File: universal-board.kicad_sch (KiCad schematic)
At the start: 38 parts, among them J1 USB_C_Receptacle, J2 Conn_02x04_Odd_Even, J3 Conn_01x08, J4 CONN_WS2812, J5 CONN_I2C_GROVE, Q1 BSS138, SW1 SW_RESET, SW2 SW_ACK, U1 USBLC6-2SC6, U2 AMS1117-3.3, U3 CH224K, U4 USBLC6-2SC6, U5 74AHCT1G125, U6 TSOP384xx, U7 ESP32-S3-WROOM-1

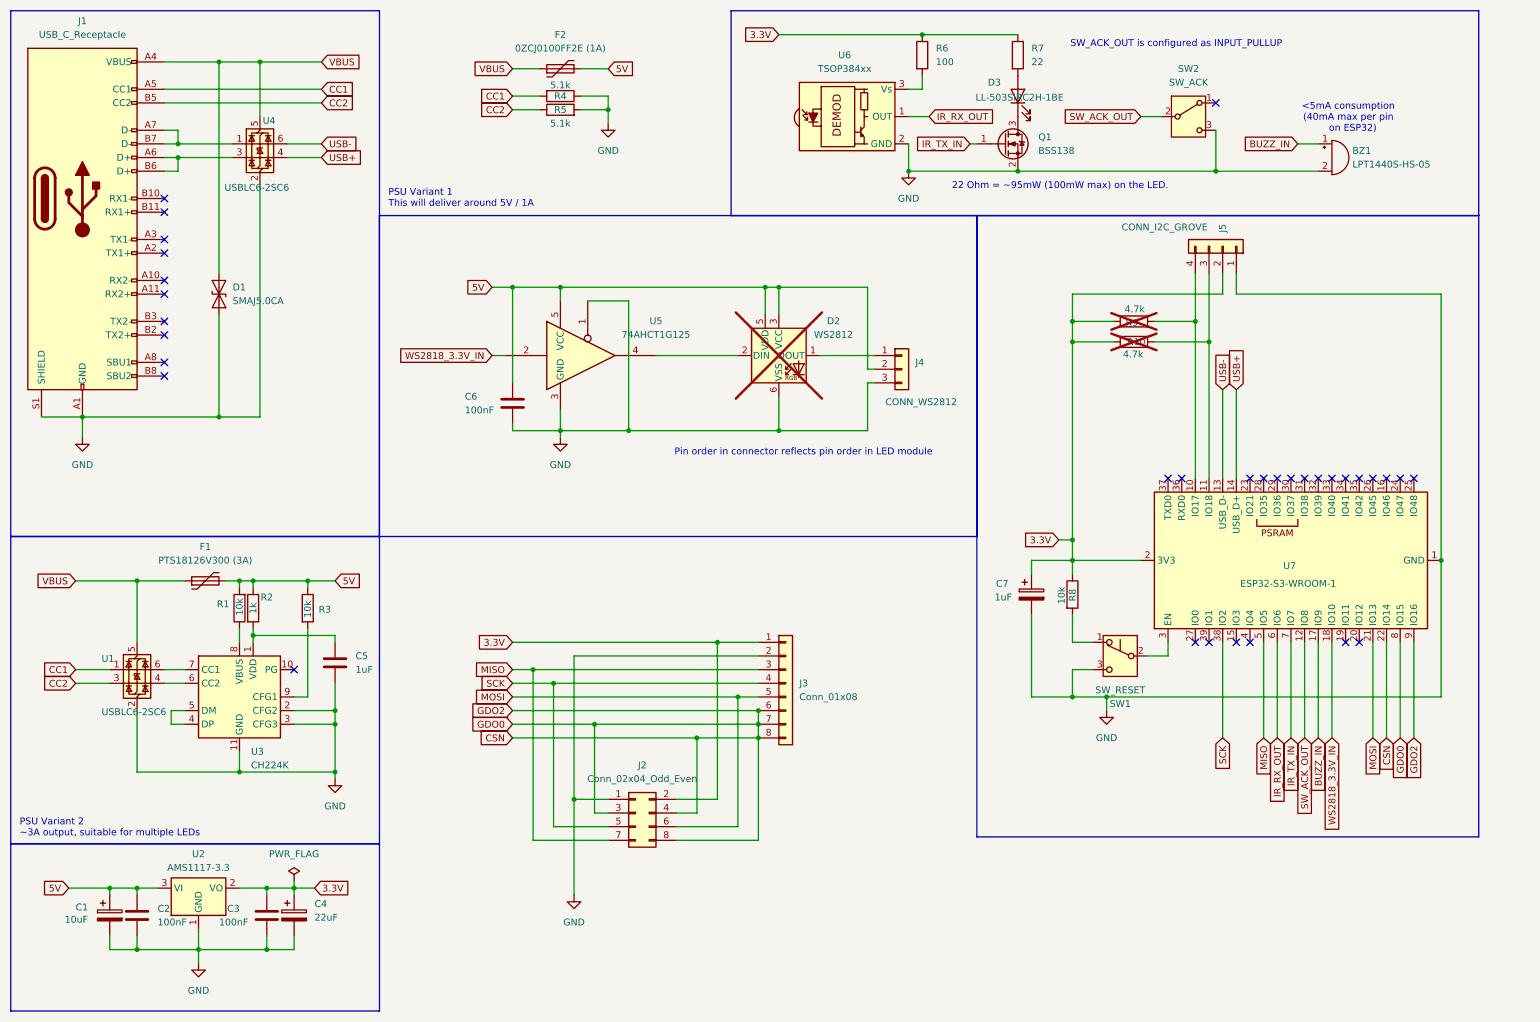
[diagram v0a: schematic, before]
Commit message: ERC checks clean.
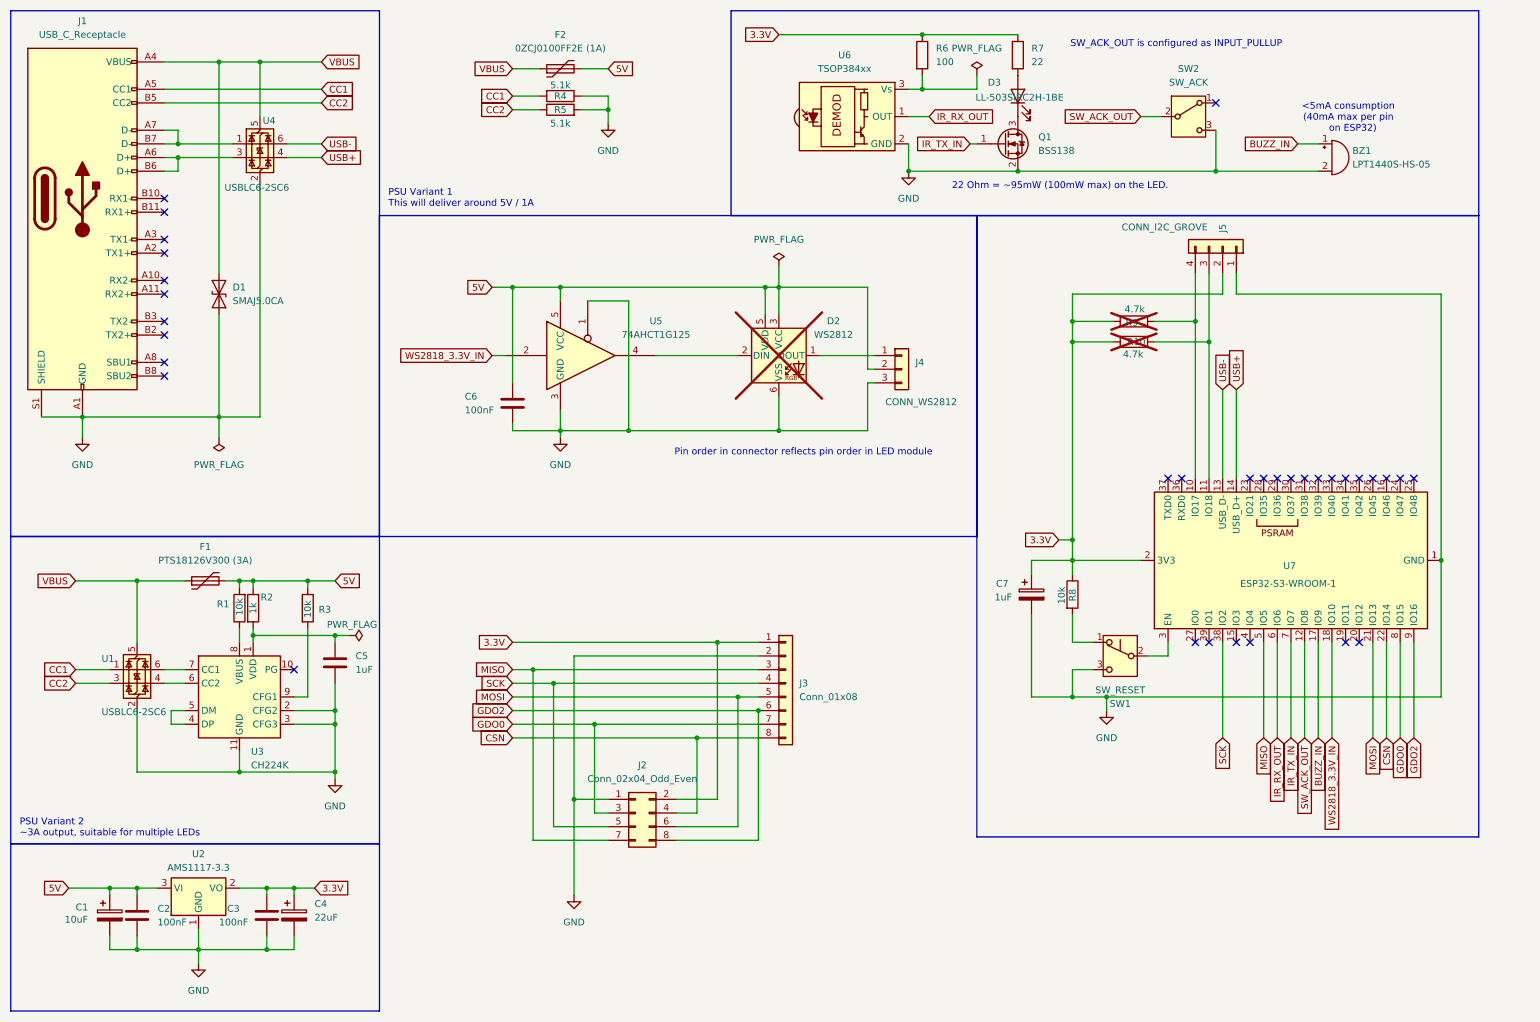
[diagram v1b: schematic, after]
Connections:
- net CSN: no longer J2.3 (Pin_3), J2.8 (Pin_8), J3.6 (Pin_6), J3.7 (Pin_7), U7.8 (IO15), U7.9 (IO16)
- new net GDO0: J2.3 (Pin_3), J3.7 (Pin_7), U7.8 (IO15)
- new net GDO2: J2.8 (Pin_8), J3.6 (Pin_6), U7.9 (IO16)

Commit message: Rev 1, added test points
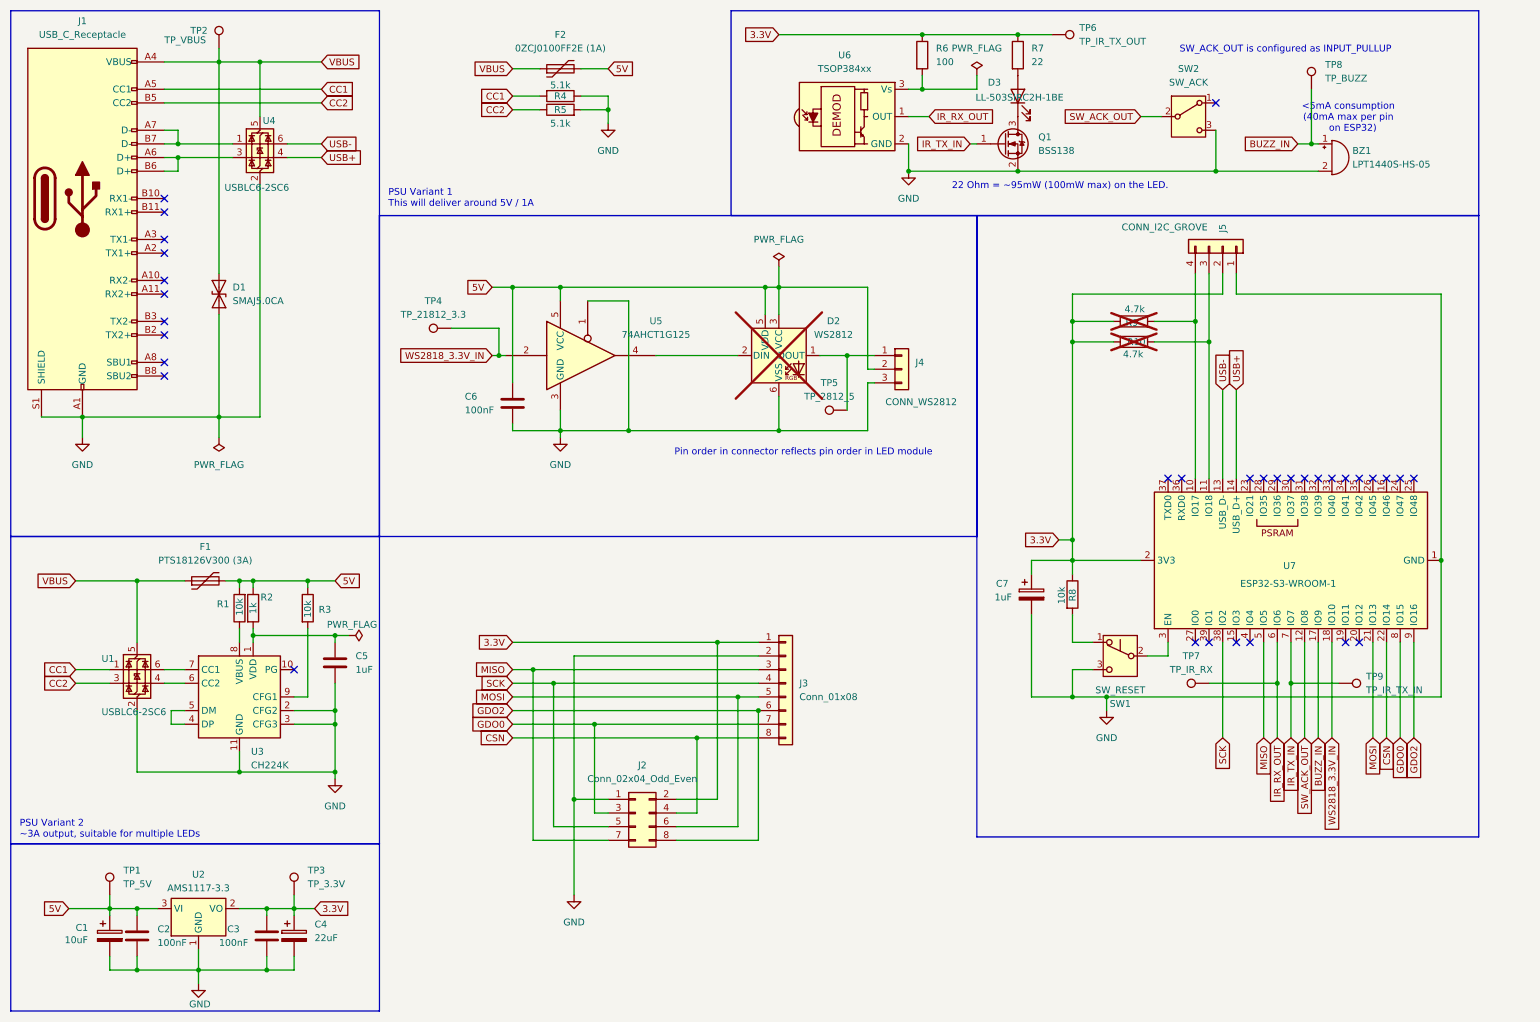
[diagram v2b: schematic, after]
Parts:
- added TP1: TP_5V, symbol Connector:TestPoint
- added TP2: TP_VBUS, symbol Connector:TestPoint
- added TP3: TP_3.3V, symbol Connector:TestPoint
- added TP4: TP_21812_3.3, symbol Connector:TestPoint
- added TP5: TP_2812_5, symbol Connector:TestPoint
- added TP6: TP_IR_TX_OUT, symbol Connector:TestPoint
- added TP7: TP_IR_RX, symbol Connector:TestPoint
- added TP8: TP_BUZZ, symbol Connector:TestPoint
- added TP9: TP_IR_TX_IN, symbol Connector:TestPoint
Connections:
- net 3.3V: now also TP3.1, TP6.1
- net 5V: now also TP1.1
- net BUZZ_IN: now also TP8.1
- net IR_RX_OUT: now also TP7.1
- net IR_TX_IN: now also TP9.1
- net VBUS: now also TP2.1
- net WS2818_3.3V_IN: now also TP4.1
- net at D2.1 (DOUT), J4.1 (Pin_1): now also TP5.1
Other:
- title: (none) -> esphome universal board
- moved on the sheet: C1, C2, C3, C4, U2

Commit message: Partial footprint assignment.
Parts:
- BZ1: footprint (none) -> Buzzer_Beeper:MagneticBuzzer_CUI_CST-931RP-A
- C1: footprint (none) -> Capacitor_THT:CP_Radial_D6.3mm_P2.50mm
- C2, C3, C5, C6, R1, R10, R2, R3, R4, R5, R6, R7, R8, R9: footprint (none) -> Capacitor_SMD:C_1206_3216Metric_Pad1.33x1.80mm_HandSolder
- C4: footprint (none) -> Capacitor_THT:CP_Radial_D5.0mm_P2.00mm
- C7: footprint (none) -> Capacitor_THT:CP_Radial_D5.0mm_P2.50mm
- D3: footprint (none) -> LED_THT:LED_D5.0mm_Clear
- F1: footprint (none) -> Fuse:Fuse_1812_4532Metric_Pad1.30x3.40mm_HandSolder
- F2: footprint (none) -> Fuse:Fuse_1206_3216Metric_Pad1.42x1.75mm_HandSolder
- SW1, SW2: footprint (none) -> Button_Switch_THT:SW_PUSH_6mm
- TP1, TP2, TP3, TP4, TP5, TP6, TP7, TP8, TP9: footprint (none) -> TestPoint:TestPoint_Pad_D2.0mm
- U5: footprint (none) -> Package_TO_SOT_SMD:SOT-353_SC-70-5_Handsoldering
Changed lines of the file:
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@@
 			)
 		)
-		(property "Footprint" ""
+		(property "Footprint" "Capacitor_SMD:C_1206_3216Metric_Pad1.33x1.80mm_HandSolder"
 			(at 207.772 120.65 90)
 			(effects
@@
 			)
 		)
-		(property "Footprint" ""
+		(property "Footprint" "Fuse:Fuse_1206_3216Metric_Pad1.42x1.75mm_HandSolder"
 			(at 119.38 21.59 0)
 			(effects
@@
 			)
 		)
-		(property "Footprint" ""
+		(property "Footprint" "LED_THT:LED_D5.0mm_Clear"
 			(at 199.39 27.94 0)
 			(effects
@@
 			)
 		)
-		(property "Footprint" ""
+		(property "Footprint" "Button_Switch_THT:SW_PUSH_6mm"
 			(at 231.14 31.75 0)
 			(effects
@@
 			)
 		)
-		(property "Footprint" ""
+		(property "Footprint" "Capacitor_THT:CP_Radial_D6.3mm_P2.50mm"
 			(at 31.4452 187.96 0)
 			(effects
@@
 			)
 		)
-		(property "Footprint" ""
+		(property "Footprint" "Fuse:Fuse_1812_4532Metric_Pad1.30x3.40mm_HandSolder"
 			(at 53.34 116.84 0)
 			(effects
@@
 			)
 		)
-		(property "Footprint" ""
+		(property "Footprint" "Button_Switch_THT:SW_PUSH_6mm"
 			(at 218.44 132.08 0)
 			(effects
@@
 			)
 		)
-		(property "Footprint" ""
+		(property "Footprint" "TestPoint:TestPoint_Pad_D2.0mm"
 			(at 55.88 19.05 0)
 			(effects
@@
 			)
 		)
-		(property "Footprint" ""
+		(property "Footprint" "TestPoint:TestPoint_Pad_D2.0mm"
 			(at 205.74 21.59 0)
 			(effects
@@
 			)
 		)
-		(property "Footprint" ""
+		(property "Footprint" "Capacitor_SMD:C_1206_3216Metric_Pad1.33x1.80mm_HandSolder"
 			(at 106.3752 88.9 0)
 			(effects
@@
 			)
 		)
-		(property "Footprint" ""
+		(property "Footprint" "Capacitor_SMD:C_1206_3216Metric_Pad1.33x1.80mm_HandSolder"
 			(at 197.612 20.32 90)
 			(effects
@@
 			)
 		)
-		(property "Footprint" ""
+		(property "Footprint" "TestPoint:TestPoint_Pad_D2.0mm"
 			(at 69.85 176.53 0)
 			(effects
@@
 			)
 		)
-		(property "Footprint" ""
+		(property "Footprint" "Capacitor_SMD:C_1206_3216Metric_Pad1.33x1.80mm_HandSolder"
 			(at 55.372 123.19 90)
 			(effects
@@
 			)
 		)
-		(property "Footprint" ""
+		(property "Footprint" "Capacitor_SMD:C_1206_3216Metric_Pad1.33x1.80mm_HandSolder"
 			(at 220.98 71.628 90)
 			(effects
@@
 			)
 		)
-		(property "Footprint" ""
+		(property "Footprint" "Capacitor_SMD:C_1206_3216Metric_Pad1.33x1.80mm_HandSolder"
 			(at 60.6552 187.96 0)
 			(effects
@@
 			)
 		)
-		(property "Footprint" ""
+		(property "Footprint" "Capacitor_SMD:C_1206_3216Metric_Pad1.33x1.80mm_HandSolder"
 			(at 220.98 71.882 90)
 			(effects
@@
 			)
 		)
-		(property "Footprint" ""
+		(property "Footprint" "TestPoint:TestPoint_Pad_D2.0mm"
 			(at 259.08 26.67 0)
 			(effects
@@
 			)
 		)
-		(property "Footprint" ""
+		(property "Footprint" "Capacitor_SMD:C_1206_3216Metric_Pad1.33x1.80mm_HandSolder"
 			(at 56.388 123.19 90)
 			(effects
@@
 			)
 		)
-		(property "Footprint" ""
+		(property "Footprint" "Capacitor_SMD:C_1206_3216Metric_Pad1.33x1.80mm_HandSolder"
 			(at 114.3 32.258 90)
 			(effects
@@
 			)
 		)
-		(property "Footprint" ""
+		(property "Footprint" "TestPoint:TestPoint_Pad_D2.0mm"
 			(at 35.56 176.53 0)
 			(effects
@@
 			)
 		)
-		(property "Footprint" ""
+		(property "Footprint" "Capacitor_SMD:C_1206_3216Metric_Pad1.33x1.80mm_HandSolder"
 			(at 114.3 26.162 90)
 			(effects
@@
 			)
 		)
-		(property "Footprint" ""
+		(property "Footprint" "Capacitor_SMD:C_1206_3216Metric_Pad1.33x1.80mm_HandSolder"
 			(at 73.3552 137.16 0)
 			(effects
@@
 			)
 		)
-		(property "Footprint" ""
+		(property "Footprint" "Buzzer_Beeper:MagneticBuzzer_CUI_CST-931RP-A"
 			(at 257.175 36.83 90)
 			(effects
@@
 			)
 		)
-		(property "Footprint" ""
+		(property "Footprint" "Capacitor_SMD:C_1206_3216Metric_Pad1.33x1.80mm_HandSolder"
 			(at 36.5252 187.96 0)
 			(effects
@@
 			)
 		)
-		(property "Footprint" ""
+		(property "Footprint" "Capacitor_THT:CP_Radial_D5.0mm_P2.00mm"
 			(at 65.7352 187.96 0)
 			(effects
@@
 			)
 		)
-		(property "Footprint" ""
+		(property "Footprint" "Capacitor_SMD:C_1206_3216Metric_Pad1.33x1.80mm_HandSolder"
 			(at 179.832 20.32 90)
 			(effects
@@
 			)
 		)
-		(property "Footprint" ""
+		(property "Footprint" "Capacitor_THT:CP_Radial_D5.0mm_P2.50mm"
 			(at 202.8952 124.46 0)
 			(effects
@@
 			)
 		)
-		(property "Footprint" ""
+		(property "Footprint" "TestPoint:TestPoint_Pad_D2.0mm"
 			(at 167.64 81.28 0)
 			(effects
@@
 			)
 		)
-		(property "Footprint" ""
+		(property "Footprint" "TestPoint:TestPoint_Pad_D2.0mm"
 			(at 259.08 142.24 0)
 			(effects
@@
 			)
 		)
-		(property "Footprint" ""
+		(property "Footprint" "TestPoint:TestPoint_Pad_D2.0mm"
 			(at 234.95 132.08 0)
 			(effects
@@
 			)
 		)
-		(property "Footprint" ""
+		(property "Footprint" "Capacitor_SMD:C_1206_3216Metric_Pad1.33x1.80mm_HandSolder"
 			(at 65.532 123.19 90)
 			(effects
@@
 			)
 		)
-		(property "Footprint" ""
+		(property "Footprint" "TestPoint:TestPoint_Pad_D2.0mm"
 			(at 93.98 66.04 0)
 			(effects
@@
 			)
 		)
-		(property "Footprint" ""
+		(property "Footprint" "Package_TO_SOT_SMD:SOT-353_SC-70-5_Handsoldering"
 			(at 119.38 76.2 0)
 			(effects

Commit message: PCB WIP
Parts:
- J1: footprint (none) -> Connector_USB:USB_C_Receptacle_GCT_USB4085
- J2: footprint (none) -> Connector_PinHeader_2.54mm:PinHeader_2x04_P2.54mm_Vertical
- J3: footprint (none) -> Connector_PinHeader_2.00mm:PinHeader_1x08_P2.00mm_Vertical
- J4: footprint (none) -> Connector_PinHeader_2.54mm:PinHeader_1x03_P2.54mm_Vertical
- J5: footprint (none) -> Connector:NS-Tech_Grove_1x04_P2mm_Vertical
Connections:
- net GND: now also SW2.1 (A); no longer SW2.3 (C)
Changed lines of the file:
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@@
 		(lib_id "Switch:SW_SPDT")
 		(at 231.14 31.75 0)
+		(mirror x)
 		(unit 1)
 		(exclude_from_sim no)
@@
 		(on_board yes)
 		(dnp no)
-		(fields_autoplaced yes)
 		(property "Reference" "SW2"
-			(at 231.14 22.86 0)
+			(at 231.14 40.64 0)
 			(effects
 				(font
@@
 		)
 		(property "Value" "SW_ACK"
-			(at 231.14 25.4 0)
+			(at 231.14 38.1 0)
 			(effects
 				(font
@@
 		)
 		(property "Datasheet" "~"
-			(at 231.14 39.37 0)
+			(at 231.14 24.13 0)
 			(effects
 				(font
@@
 			)
 		)
-		(property "Footprint" ""
+		(property "Footprint" "Connector_PinHeader_2.54mm:PinHeader_1x03_P2.54mm_Vertical"
 			(at 177.8 78.74 0)
 			(effects
@@
 			)
 		)
-		(property "Footprint" ""
+		(property "Footprint" "Connector:NS-Tech_Grove_1x04_P2mm_Vertical"
 			(at 237.49 55.88 0)
 			(effects
@@
 			)
 		)
-		(property "Footprint" ""
+		(property "Footprint" "Connector_USB:USB_C_Receptacle_GCT_USB4085"
 			(at 29.21 46.99 0)
 			(effects
@@
 			)
 		)
-		(property "Footprint" ""
+		(property "Footprint" "Connector_PinHeader_2.54mm:PinHeader_2x04_P2.54mm_Vertical"
 			(at 128.27 161.29 0)
 			(effects
@@
 			)
 		)
-		(property "Footprint" ""
+		(property "Footprint" "Connector_PinHeader_2.00mm:PinHeader_1x08_P2.00mm_Vertical"
 			(at 156.21 137.16 0)
 			(effects
